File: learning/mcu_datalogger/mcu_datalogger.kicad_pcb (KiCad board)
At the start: 2 copper layers, 0 parts

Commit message: Added all the footprints to the pcb editor
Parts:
- added BT1: Battery, Connector_PinHeader_2.54mm:PinHeader_1x02_P2.54mm_Vertical, F.Cu at (102.9, 80.0)
- added C1: 0.1u, Capacitor_SMD:C_0805_2012Metric, F.Cu at (120.3, 73.7)
- added C2: 22p, Capacitor_SMD:C_0805_2012Metric, F.Cu at (133.7, 90.2)
- added C3: 22p, Capacitor_SMD:C_0805_2012Metric, F.Cu at (124.8, 73.7)
- added C4: 0.1u, Capacitor_SMD:C_0805_2012Metric, F.Cu at (133.7, 94.0)
- added C5: 100n, Capacitor_SMD:C_0805_2012Metric, F.Cu at (129.2, 73.7)
- added D1: LED, LED_SMD:LED_0805_2012Metric, F.Cu at (138.1, 73.7)
- added D2: LED, LED_SMD:LED_0805_2012Metric, F.Cu at (133.7, 73.7)
- added H1: MountingHole, MountingHole:MountingHole_2.1mm, F.Cu at (101.6, 73.7)
- added H2: MountingHole, MountingHole:MountingHole_2.1mm, F.Cu at (101.6, 99.1)
- added H3: MountingHole, MountingHole:MountingHole_2.1mm, F.Cu at (147.3, 73.7)
- added H4: MountingHole, MountingHole:MountingHole_2.1mm, F.Cu at (147.3, 99.1)
- added J1: Conn_01x09_Pin, Connector_PinHeader_2.54mm:PinHeader_1x09_P2.54mm_Vertical, F.Cu at (106.7, 98.4)
- added J2: Conn_01x04_Pin, Connector_PinHeader_2.54mm:PinHeader_1x04_P2.54mm_Vertical, F.Cu at (145.4, 87.0)
- added J3: Conn_01x04_Pin, Connector_PinHeader_2.54mm:PinHeader_1x04_P2.54mm_Vertical, F.Cu at (132.7, 98.4)
- added J4: Conn_02x03_Odd_Even, Connector_PinHeader_2.54mm:PinHeader_2x03_P2.54mm_Vertical, F.Cu at (142.9, 78.1)
- added R1: 10k, Resistor_SMD:R_0805_2012Metric, F.Cu at (110.1, 94.6)
- added R2: 10k, Resistor_SMD:R_0805_2012Metric, F.Cu at (114.7, 94.6)
- added R3: 4.7k, Resistor_SMD:R_0805_2012Metric, F.Cu at (133.7, 86.4)
- added R4: 4.7k, Resistor_SMD:R_0805_2012Metric, F.Cu at (133.7, 82.5)
- added R5: 330, Resistor_SMD:R_0805_2012Metric, F.Cu at (138.1, 78.1)
- added R6: 10k, Resistor_SMD:R_0805_2012Metric, F.Cu at (138.1, 82.5)
- added R7: 330, Resistor_SMD:R_0805_2012Metric, F.Cu at (133.7, 78.1)
- added U1: 24LC1025, Package_SO:SOIC-8_5.3x5.3mm_P1.27mm, F.Cu at (112.4, 75.6)
- added U2: DS1337S_, DS1337S_:SOIC127P600X175-8N, F.Cu at (112.4, 89.5)
- added U3: 24LC1025, Package_SO:SOIC-8_5.3x5.3mm_P1.27mm, F.Cu at (112.4, 82.5)
- added U4: ATMEGA328P-AU, Atmega328p-au:QFP80P900X900X120-32N, F.Cu at (124.5, 83.2)
- added Y1: 16MHz, Crystal:Crystal_SMD_5032-2Pin_5.0x3.2mm_HandSoldering, F.Cu at (102.9, 90.9)
- added Y2: 32.768kHz, Crystal:Crystal_SMD_5032-2Pin_5.0x3.2mm_HandSoldering, F.Cu at (124.4, 92.7)
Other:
- board outline added: 50.8 x 30.5 mm

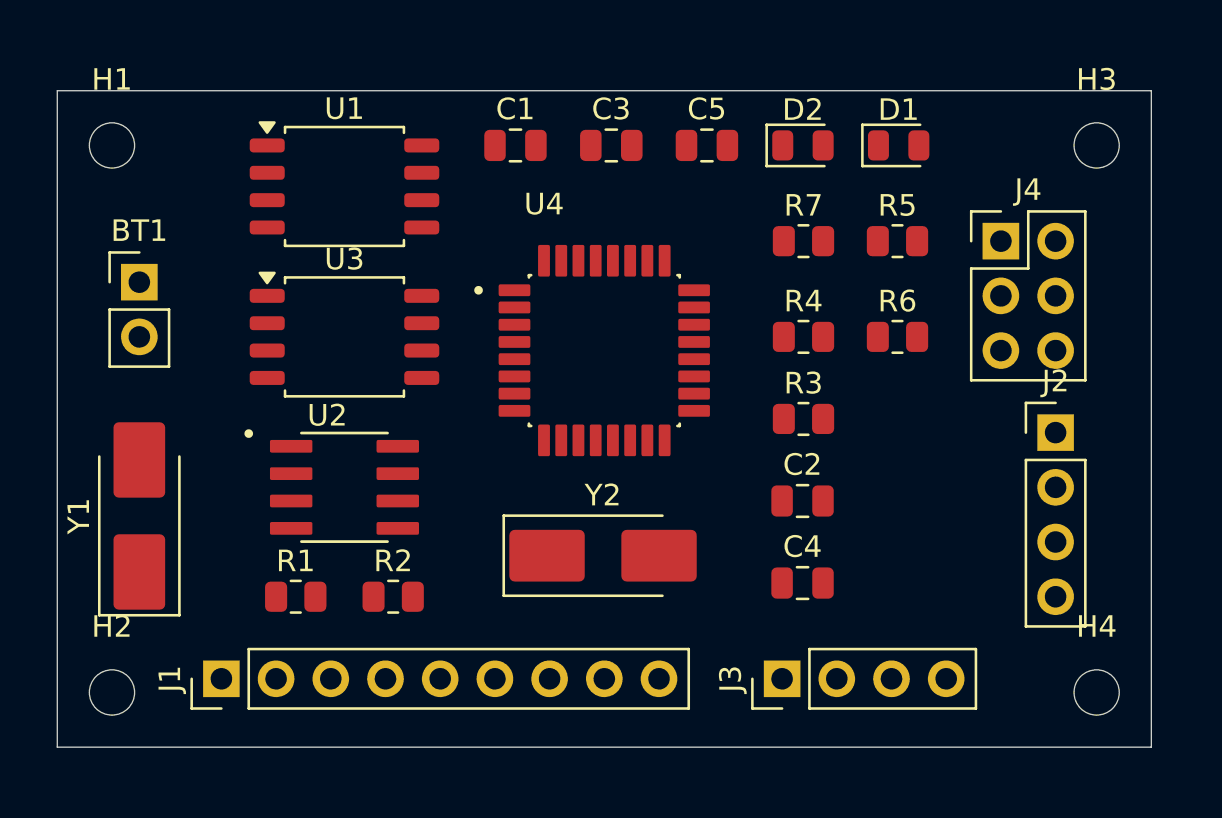
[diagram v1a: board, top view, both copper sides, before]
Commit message: Redefined shape and layout
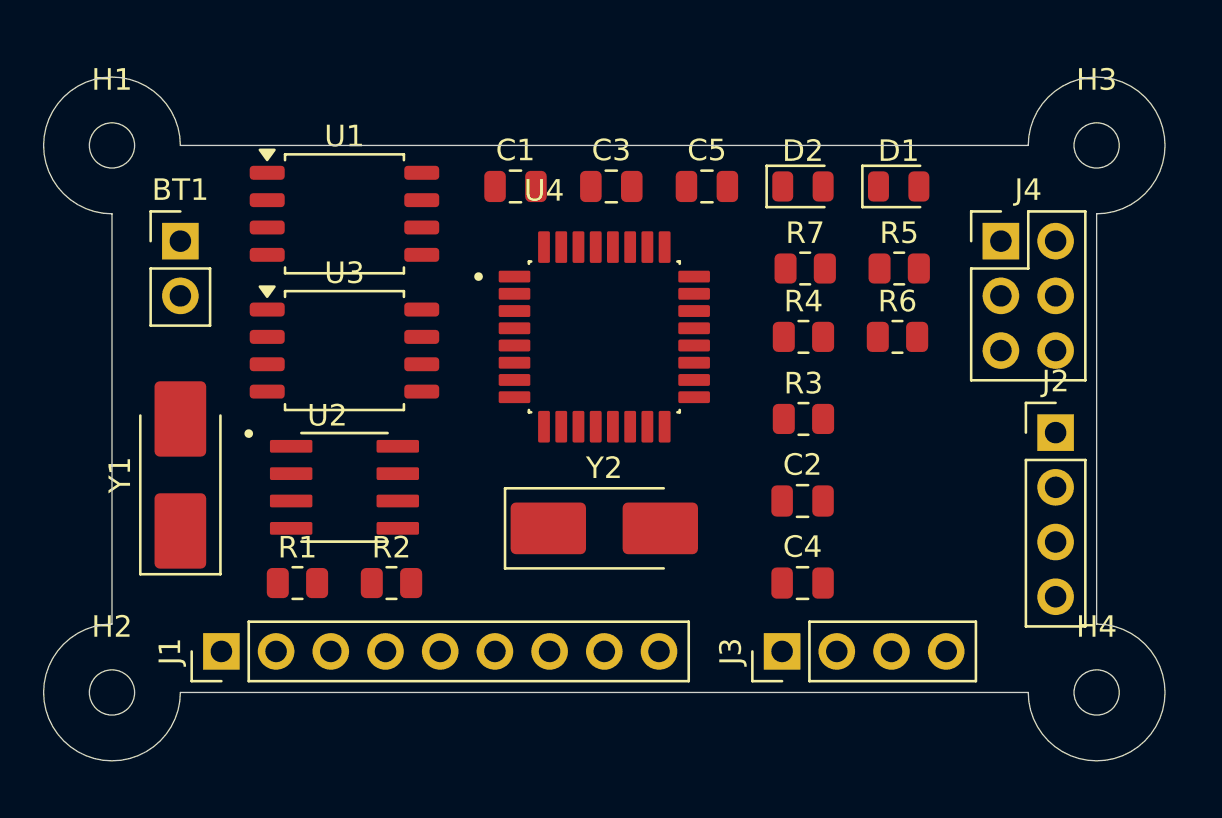
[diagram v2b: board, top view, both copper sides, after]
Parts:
- moved BT1 2.69 mm to (104.8, 78.1)
- moved Y1 2.69 mm to (104.8, 89.0)
- moved C1 1.91 mm to (120.3, 75.6)
- moved C3 1.91 mm to (124.8, 75.6)
- moved C5 1.91 mm to (129.2, 75.6)
- moved D1 1.91 mm to (138.1, 75.6)
- moved D2 1.91 mm to (133.7, 75.6)
- moved R5 1.27 mm to (138.2, 79.4)
- moved R7 1.27 mm to (133.8, 79.4)
- moved Y2 1.27 mm to (124.5, 91.4)
- moved J1 1.27 mm to (106.7, 97.2)
- moved J3 1.27 mm to (132.7, 97.2)
- moved U1 1.27 mm to (112.4, 76.8)
- moved R1 0.64 mm to (110.2, 94.0)
- moved R2 0.64 mm to (114.6, 94.0)
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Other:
- board size 50.8 x 30.5 mm -> 52.1 x 31.7 mm
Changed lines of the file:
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@@
 	(footprint "Capacitor_SMD:C_0805_2012Metric"
 		(layer "F.Cu")
-		(at 129.225 73.66)
+		(at 129.225 75.565)
 		(descr "Capacitor SMD 0805 (2012 Metric), square (rectangular) end terminal, IPC-7351 nominal, (Body size source: IPC-SM-782 page 76, https://www.pcb-3d.com/wordpress/wp-content/uploads/ipc-sm-782a_amendment_1_and_2.pdf, https://docs.google.com/spreadsheets/d/1BsfQQcO9C6DZCsRaXUlFlo91Tg2WpOkGARC1WS5S8t0/edit?usp=sharing), generated with kicad-footprint-generator")
 		(tags "capacitor")
@@
 	(footprint "Connector_PinHeader_2.54mm:PinHeader_1x04_P2.54mm_Vertical"
 		(layer "F.Cu")
-		(at 132.715 98.425 90)
+		(at 132.715 97.155 90)
 		(descr "Through hole straight pin header, 1x04, 2.54mm pitch, single row")
 		(tags "Through hole pin header THT 1x04 2.54mm single row")
@@
 	(footprint "Resistor_SMD:R_0805_2012Metric"
 		(layer "F.Cu")
-		(at 114.6575 94.615)
+		(at 114.5775 93.98)
 		(descr "Resistor SMD 0805 (2012 Metric), square (rectangular) end terminal, IPC-7351 nominal, (Body size source: IPC-SM-782 page 72, https://www.pcb-3d.com/wordpress/wp-content/uploads/ipc-sm-782a_amendment_1_and_2.pdf), generated with kicad-footprint-generator")
 		(tags "resistor")
@@
 	(footprint "Package_SO:SOIC-8_5.3x5.3mm_P1.27mm"
 		(layer "F.Cu")
-		(at 112.395 75.565)
+		(at 112.395 76.835)
 		(descr "SOIC, 8 Pin (JEITA/EIAJ ED-7311-19 variation 08-001-BBA and Atmel/Microchip, 208 mils width, https://www.jeita.or.jp/japanese/standard/book/ED-7311-19/#target/page_no=21, https://ww1.microchip.com/downloads/en/DeviceDoc/20005045C.pdf#page=23, https://ww1.microchip.com/downloads/en/DeviceDoc/doc2535.pdf#page=162), generated with kicad-footprint-generator ipc_gullwing_generator.py")
 		(tags "SOIC SO P-SOP SOP SOP-8 SO SO-8 8S2 S2AE/F K04-056 CASE-751BE SO8W 8-Pin-SOIC PSA W8-2 W8-4 W8MS-1 FPT-8P-M08")
@@
 	(footprint "Capacitor_SMD:C_0805_2012Metric"
 		(layer "F.Cu")
-		(at 120.335 73.66)
+		(at 120.335 75.565)
 		(descr "Capacitor SMD 0805 (2012 Metric), square (rectangular) end terminal, IPC-7351 nominal, (Body size source: IPC-SM-782 page 76, https://www.pcb-3d.com/wordpress/wp-content/uploads/ipc-sm-782a_amendment_1_and_2.pdf, https://docs.google.com/spreadsheets/d/1BsfQQcO9C6DZCsRaXUlFlo91Tg2WpOkGARC1WS5S8t0/edit?usp=sharing), generated with kicad-footprint-generator")
 		(tags "capacitor")
@@
 	(footprint "Crystal:Crystal_SMD_5032-2Pin_5.0x3.2mm_HandSoldering"
 		(layer "F.Cu")
-		(at 124.4 92.71)
+		(at 124.46 91.44)
 		(descr "SMD2520/2, Crystal, 5.0x3.2mm package, SMD, hand-soldering, generated with kicad-footprint-generator make_crystal.py, http://www.icbase.com/File/PDF/HKC/HKC00061008.pdf")
 		(property "Reference" "Y2"
@@
 	(footprint "Crystal:Crystal_SMD_5032-2Pin_5.0x3.2mm_HandSoldering"
 		(layer "F.Cu")
-		(at 102.87 90.865 90)
+		(at 104.775 88.96 90)
 		(descr "SMD2520/2, Crystal, 5.0x3.2mm package, SMD, hand-soldering, generated with kicad-footprint-generator make_crystal.py, http://www.icbase.com/File/PDF/HKC/HKC00061008.pdf")
 		(property "Reference" "Y1"
@@
 	(footprint "Package_SO:SOIC-8_5.3x5.3mm_P1.27mm"
 		(layer "F.Cu")
-		(at 112.395 82.55)
+		(at 112.395 83.185)
 		(descr "SOIC, 8 Pin (JEITA/EIAJ ED-7311-19 variation 08-001-BBA and Atmel/Microchip, 208 mils width, https://www.jeita.or.jp/japanese/standard/book/ED-7311-19/#target/page_no=21, https://ww1.microchip.com/downloads/en/DeviceDoc/20005045C.pdf#page=23, https://ww1.microchip.com/downloads/en/DeviceDoc/doc2535.pdf#page=162), generated with kicad-footprint-generator ipc_gullwing_generator.py")
 		(tags "SOIC SO P-SOP SOP SOP-8 SO SO-8 8S2 S2AE/F K04-056 CASE-751BE SO8W 8-Pin-SOIC PSA W8-2 W8-4 W8MS-1 FPT-8P-M08")
@@
 	(footprint "Resistor_SMD:R_0805_2012Metric"
 		(layer "F.Cu")
-		(at 133.7075 78.105)
+		(at 133.7875 79.375)
 		(descr "Resistor SMD 0805 (2012 Metric), square (rectangular) end terminal, IPC-7351 nominal, (Body size source: IPC-SM-782 page 72, https://www.pcb-3d.com/wordpress/wp-content/uploads/ipc-sm-782a_amendment_1_and_2.pdf), generated with kicad-footprint-generator")
 		(tags "resistor")
@@
 	(footprint "Resistor_SMD:R_0805_2012Metric"
 		(layer "F.Cu")
-		(at 110.1325 94.615)
+		(at 110.2125 93.98)
 		(descr "Resistor SMD 0805 (2012 Metric), square (rectangular) end terminal, IPC-7351 nominal, (Body size source: IPC-SM-782 page 72, https://www.pcb-3d.com/wordpress/wp-content/uploads/ipc-sm-782a_amendment_1_and_2.pdf), generated with kicad-footprint-generator")
 		(tags "resistor")
@@
 	(footprint "Connector_PinHeader_2.54mm:PinHeader_1x09_P2.54mm_Vertical"
 		(layer "F.Cu")
-		(at 106.68 98.425 90)
+		(at 106.68 97.155 90)
 		(descr "Through hole straight pin header, 1x09, 2.54mm pitch, single row")
 		(tags "Through hole pin header THT 1x09 2.54mm single row")
@@
 	(footprint "LED_SMD:LED_0805_2012Metric"
 		(layer "F.Cu")
-		(at 138.1275 73.66)
+		(at 138.1275 75.565)
 		(descr "LED SMD 0805 (2012 Metric), square (rectangular) end terminal, IPC-7351 nominal, (Body size source: https://docs.google.com/spreadsheets/d/1BsfQQcO9C6DZCsRaXUlFlo91Tg2WpOkGARC1WS5S8t0/edit?usp=sharing), generated with kicad-footprint-generator")
 		(tags "LED")
@@
 	(footprint "Capacitor_SMD:C_0805_2012Metric"
 		(layer "F.Cu")
-		(at 124.785 73.66)
+		(at 124.785 75.565)
 		(descr "Capacitor SMD 0805 (2012 Metric), square (rectangular) end terminal, IPC-7351 nominal, (Body size source: IPC-SM-782 page 76, https://www.pcb-3d.com/wordpress/wp-content/uploads/ipc-sm-782a_amendment_1_and_2.pdf, https://docs.google.com/spreadsheets/d/1BsfQQcO9C6DZCsRaXUlFlo91Tg2WpOkGARC1WS5S8t0/edit?usp=sharing), generated with kicad-footprint-generator")
 		(tags "capacitor")
@@
 	(footprint "LED_SMD:LED_0805_2012Metric"
 		(layer "F.Cu")
-		(at 133.6825 73.66)
+		(at 133.6825 75.565)
 		(descr "LED SMD 0805 (2012 Metric), square (rectangular) end terminal, IPC-7351 nominal, (Body size source: https://docs.google.com/spreadsheets/d/1BsfQQcO9C6DZCsRaXUlFlo91Tg2WpOkGARC1WS5S8t0/edit?usp=sharing), generated with kicad-footprint-generator")
 		(tags "LED")
@@
 	(footprint "Resistor_SMD:R_0805_2012Metric"
 		(layer "F.Cu")
-		(at 138.0725 78.105)
+		(at 138.1525 79.375)
 		(descr "Resistor SMD 0805 (2012 Metric), square (rectangular) end terminal, IPC-7351 nominal, (Body size source: IPC-SM-782 page 72, https://www.pcb-3d.com/wordpress/wp-content/uploads/ipc-sm-782a_amendment_1_and_2.pdf), generated with kicad-footprint-generator")
 		(tags "resistor")
@@
 	(footprint "Atmega328p-au:QFP80P900X900X120-32N"
 		(layer "F.Cu")
-		(at 124.46 83.185)
+		(at 124.46 82.55)
 		(property "Reference" "U4"
 			(at -2.795 -6.79 0)
@@
 	(footprint "Connector_PinHeader_2.54mm:PinHeader_1x02_P2.54mm_Vertical"
 		(layer "F.Cu")
-		(at 102.87 80.01)
+		(at 104.775 78.105)
 		(descr "Through hole straight pin header, 1x02, 2.54mm pitch, single row")
 		(tags "Through hole pin header THT 1x02 2.54mm single row")
@@
 		)
 	)
-	(gr_rect
-		(start 99.06 71.12)
-		(end 149.86 101.6)
+	(gr_line
+		(start 144.145 73.66)
+		(end 104.775 73.66)
+		(stroke
+			(width 0.05)
+			(type default)
+		)
+		(layer "Edge.Cuts")
+	)
+	(gr_arc
+		(start 104.775 99.06)
+		(mid 99.354936 101.305064)
+		(end 101.6 95.885)
+		(stroke
+			(width 0.05)
+			(type default)
+		)
+		(layer "Edge.Cuts")
+	)
+	(gr_line
+		(start 101.6 95.885)
+		(end 101.6 95.885)
+		(stroke
+			(width 0.05)
+			(type default)
+		)
+		(layer "Edge.Cuts")
+	)
+	(gr_arc
+		(start 101.6 76.835)
+		(mid 99.354936 71.414936)
+		(end 104.775 73.66)
+		(stroke
+			(width 0.05)
+			(type default)
+		)
+		(layer "Edge.Cuts")
+	)
+	(gr_line
+		(start 147.32 95.885)
+		(end 147.32 76.835)
+		(stroke
+			(width 0.05)
+			(type default)
+		)
+		(layer "Edge.Cuts")
+	)
+	(gr_line
+		(start 101.6 76.835)
+		(end 101.6 95.885)
+		(stroke
+			(width 0.05)
+			(type default)
+		)
+		(layer "Edge.Cuts")
+	)
+	(gr_arc
+		(start 147.32 95.885)
+		(mid 149.565064 101.305064)
+		(end 144.145 99.06)
+		(stroke
+			(width 0.05)
+			(type default)
+		)
+		(layer "Edge.Cuts")
+	)
+	(gr_line
+		(start 104.775 99.06)
+		(end 144.145 99.06)
+		(stroke
+			(width 0.05)
+			(type default)
+		)
+		(layer "Edge.Cuts")
+	)
+	(gr_arc
+		(start 144.145 73.66)
+		(mid 149.565064 71.414936)
+		(end 147.32 76.835)
 		(stroke
 			(width 0.05)
 			(type default)
 		)
-		(fill no)
 		(layer "Edge.Cuts")
 	)

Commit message: Finished layout of the pcb
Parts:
- moved Y1 20.7 mm to (125.3, 91.9), turned to 180 degrees
- moved Y2 19.9 mm to (104.6, 89.3), turned to 90 degrees
- moved H4 0.88 mm to (147.9, 99.7)
- moved C4 0.85 mm to (133.6, 93.1)
- moved H3 0.84 mm to (147.9, 73.0)
- moved H1 0.67 mm to (101.6, 73.0)
- moved U2 0.66 mm to (112.2, 88.9)
- moved H2 0.64 mm to (101.6, 99.7)
- moved U4 0.59 mm to (124.9, 83.0)
- moved R2 0.53 mm to (114.4, 93.5), turned to 180 degrees
- moved R1 0.52 mm to (110.1, 93.5)
- moved U1 0.44 mm to (112.2, 76.4)
- moved U3 0.41 mm to (112.2, 82.8)
- turned C2 to 180 degrees
- turned C5 to 180 degrees
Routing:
- net /Vcc: track 0.00 -> 164.6 mm, vias 0 -> 5
- net GND: track 0.00 -> 95.9 mm, vias 0 -> 6
- net /SCK: track 0.00 -> 94.1 mm, vias 0 -> 4
- net /SDA: track 0.00 -> 67.9 mm, vias 0 -> 5
- net Net-(U4-PB7): track 0.00 -> 56.6 mm, vias 0 -> 3
- net Net-(BT1-+): track 0.00 -> 55.7 mm, vias 0 -> 4
- net /TX: track 0.00 -> 33.1 mm, vias 0 -> 2
- net /D2: track 0.00 -> 30.5 mm
- net /RX: track 0.00 -> 30.1 mm, vias 0 -> 2
- net /D3: track 0.00 -> 26.5 mm
- net Net-(U4-PB6): track 0.00 -> 25.7 mm, vias 0 -> 2
- net /D4: track 0.00 -> 23.5 mm
- net /MOSI: track 0.00 -> 22.7 mm, vias 0 -> 1
- net /RESET: track 0.00 -> 22.3 mm, vias 0 -> 2
- net /MISO: track 0.00 -> 19.7 mm, vias 0 -> 1
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- added copper zone on F.Cu, net /Vcc
- added copper zone on B.Cu, net GND
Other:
- board size 52.1 x 31.7 mm -> 52.7 x 33 mm

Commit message: Finished the project
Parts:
- added G***: LOGO, PCB_Designs:my_logo, B.Cu at (110.2, 86.6)
- added REF**: KiCad-Logo2_5mm_SilkScreen, Symbol:KiCad-Logo2_5mm_SilkScreen, B.Cu at (112.2, 91.4)
- moved C4 0.09 mm to (133.6, 93.2)
- moved C2 0.07 mm to (133.6, 90.2)
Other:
- board text added: "MCU Datalogger"
- board text added: "by"
- board text added: "version:1"

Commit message: Fixed track width issues
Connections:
- BT1 pad 1: Net-(BT1-+) -> /Vcc
- C5 pad 1: Net-(BT1-+) -> /Vcc
- D2 pad 2: Net-(BT1-+) -> /Vcc
- U4 pad 18: Net-(BT1-+) -> /Vcc
- U4 pad 4: Net-(BT1-+) -> /Vcc
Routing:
- net Net-(BT1-+): track 55.7 -> 0.00 mm, vias 4 -> 0
- net /Vcc: track 164.6 -> 215.9 mm, vias 5 -> 9
- net /SCK: track 94.1 -> 94.8 mm
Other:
- board text added: "2"
- board text added: "3"
- board text added: "4"
- board text added: "5"
- board text added: "6"
- board text added: "7"
- board text added: "8"
- board text added: "GND"
- board text added: "ICSP"
- board text added: "RX"
- board text added: "SCK"
- board text added: "SDA"
- board text added: "TX"
- board text added: "Vcc"

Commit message: Completed last check and generated gerber files
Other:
- board text added: "0.0000 mm / 0.0000 mm"
- board text added: "0.3000 mm"
- board text added: "1.6000 mm"
- board text added: "52.7000 mm x 33.0150 mm"
- board text added: "BOARD CHARACTERISTICS"
- board text added: "Board Thickness:"
- board text added: "Board overall dimensions:"
- board text added: "Castellated pads:"
- board text added: "Copper Finish:"
- board text added: "Copper Layer Count:"
- board text added: "Edge card connectors:"
- board text added: "Impedance Control:"
- board text added: "Min hole diameter:"
- board text added: "Min track/spacing:"
- board text added: "No"
- board text added: "None"
- board text added: "Plated Board Edge:"
